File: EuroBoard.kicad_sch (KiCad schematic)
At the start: 35 parts, among them J1 GPIO, J10 PD1, J11 PD2, J12 PD3, J2 Conn_01x07_Male, J3 I2C, J4 Conn_01x05_Male, J5 RX, J6 TX, J7 GND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

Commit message: Rework
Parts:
- removed C1, C7: C, Capacitor_SMD:C_0805_2012Metric_Pad1.18x1.45mm_HandSolder, symbol Device:C
- removed C11: 10u, Capacitor_SMD:C_0805_2012Metric_Pad1.18x1.45mm_HandSolder, symbol Device:C
- removed C2, C8: 100n, Capacitor_SMD:C_0805_2012Metric_Pad1.18x1.45mm_HandSolder, symbol Device:C
- removed J1: GPIO, Connector_PinHeader_2.54mm:PinHeader_1x08_P2.54mm_Vertical, symbol Connector:Conn_01x08_Male
- removed J10: PD1, TestPoint:TestPoint_Pad_1.0x1.0mm, symbol Connector:Conn_01x01_Male
- removed J11: PD2, TestPoint:TestPoint_Pad_1.0x1.0mm, symbol Connector:Conn_01x01_Male
- removed J12: PD3, TestPoint:TestPoint_Pad_1.0x1.0mm, symbol Connector:Conn_01x01_Male
- removed J2: Conn_01x07_Male, Connector_PinHeader_2.54mm:PinHeader_1x07_P2.54mm_Vertical, symbol Connector:Conn_01x07_Male
- removed J3: I2C, Connector_PinHeader_2.54mm:PinHeader_1x03_P2.54mm_Vertical, symbol Connector:Conn_01x03_Male
- removed J4: Conn_01x05_Male, Connector_PinHeader_2.54mm:PinHeader_1x05_P2.54mm_Vertical, symbol Connector:Conn_01x05_Male
- removed J5: RX, TestPoint:TestPoint_Pad_1.0x1.0mm, symbol Connector:Conn_01x01_Male
- removed J6: TX, TestPoint:TestPoint_Pad_1.0x1.0mm, symbol Connector:Conn_01x01_Male
- removed J7: GND, TestPoint:TestPoint_Pad_1.0x1.0mm, symbol Connector:Conn_01x01_Male
- removed R1: R, Resistor_SMD:R_0805_2012Metric_Pad1.20x1.40mm_HandSolder, symbol Device:R
- removed R2: 1k, Resistor_SMD:R_0805_2012Metric_Pad1.20x1.40mm_HandSolder, symbol Device:R
- added C1, C5: 8p, Capacitor_SMD:C_0805_2012Metric_Pad1.18x1.45mm_HandSolder, symbol Device:C_Small
- added C2, C7: 100n, Capacitor_SMD:C_0805_2012Metric_Pad1.18x1.45mm_HandSolder, symbol Device:C_Small
- added C8: 10u, Capacitor_SMD:C_0805_2012Metric_Pad1.18x1.45mm_HandSolder, symbol Device:C_Small
- added R1, R2, R4: 0R, Capacitor_SMD:C_0805_2012Metric_Pad1.18x1.45mm_HandSolder, symbol Device:R_Small
- added R5: 1k, Resistor_SMD:R_0805_2012Metric_Pad1.20x1.40mm_HandSolder, symbol Device:R_Small
- added TP1: SPI1_SCK, MEMS_Custom:TestPoint_Pad_D1.0mm, symbol Connector:TestPoint
- added TP10: GP0, MEMS_Custom:TestPoint_Pad_D1.0mm, symbol Connector:TestPoint
- added TP11, TP12, TP13, TP14, TP15: GND, MEMS_Custom:TestPoint_Pad_D1.0mm, symbol Connector:TestPoint
- added TP16: 3V3, MEMS_Custom:TestPoint_Pad_D1.0mm, symbol Connector:TestPoint
- added TP2: SPI1_MISO, MEMS_Custom:TestPoint_Pad_D1.0mm, symbol Connector:TestPoint
- added TP3: SPI1_MOSI, MEMS_Custom:TestPoint_Pad_D1.0mm, symbol Connector:TestPoint
- added TP4: SCL_INT, MEMS_Custom:TestPoint_Pad_D1.0mm, symbol Connector:TestPoint
- added TP5: SDA_INT, MEMS_Custom:TestPoint_Pad_D1.0mm, symbol Connector:TestPoint
- added TP6: TRG, MEMS_Custom:TestPoint_Pad_D1.0mm, symbol Connector:TestPoint
- added TP7: RDY, MEMS_Custom:TestPoint_Pad_D1.0mm, symbol Connector:TestPoint
- added TP8: GP2, MEMS_Custom:TestPoint_Pad_D1.0mm, symbol Connector:TestPoint
- added TP9: GP1, MEMS_Custom:TestPoint_Pad_D1.0mm, symbol Connector:TestPoint
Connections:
- net SCL2 is gone; now on net GP2: U2.22 (PB10)
- net SDA2 is gone; now on net GP1: U2.23 (PB11)
- net +3.3V: now also C4.1, C6.1, L1.1, U1.2 (VO), TP16.1; no longer L1.2, U2.4 (VBAT), U2.6 (VDD/VDDA)
- net GND: now also C1.2, C2.2, C5.2, C7.2, C8.2, TP11.1, TP12.1, TP13.1, TP14.1, TP15.1
- net GP0: now also U2.24 (PB12), TP10.1; no longer U2.33 (PA11)
- net GP1: now also TP9.1; no longer U2.34 (PA12)
- net GP2: now also TP8.1; no longer U2.21 (PB2)
- net RDY: now also U2.48 (PB9), TP7.1; no longer U2.20 (PB1)
- net SPI1_MISO: now also TP2.1
- net SPI1_MOSI: now also TP3.1
- net SPI1_SCK: now also U2.16 (PA5), TP1.1; no longer U2.12 (PA1)
- net TRG: now also U2.47 (PB8), TP6.1; no longer U2.19 (PB0)
- net at D2.2 (A), SW1.2 (B), U2.10 (NRST): now also C2.1
- net PA0: now reaches U2.11 (PA0)
- net PA4: now reaches U2.15 (PA4)
- net at D1.2 (A): now also R5.1
- net at U2.2 (OSC32_IN/PC14): now also Y1.3, C1.1
- net at SW2.4: now also U2.38 (PD0); no longer U2.24 (PB12)
- net at SW2.3: now also U2.39 (PD1); no longer U2.25 (PB13)
- net at SW2.2: now also U2.40 (PD2); no longer U2.26 (PB14)
- net at SW2.1: now also U2.41 (PD3); no longer U2.27 (PB15)
- net PA8: now reaches U2.28 (PA8)
- net at U2.3 (OSC32_OUT/PC15): now also R4.2
- net PB6: now reaches U2.30 (PC6)
- net at U2.31 (PC7): now also R5.2
- net PA15: now reaches U2.37 (PA15)
- net PB3: now reaches U2.42 (PB3)
- net PB4: now reaches U2.43 (PB4)
- net PB5: now reaches U2.44 (PB5)
- net at Y1.1: now also C5.1, R4.1
- net LED renamed PC13
- net OSC_IN renamed PF0
- net PF0: no longer Y1.3
- net OSC_OUT renamed PF1
- net RX_AUX renamed PA10
- net SCL renamed SCL_EXT
- net SCL_EXT: now also R1.1
- net SDA renamed SDA_EXT
- net SDA_EXT: now also R2.2
- net TX_AUX renamed PA9
- net VREF: no longer names the net of U2.5 (VREF+)
- net VREF: now also C7.1
- new net: C8.1, L1.2, U2.4 (VBAT), U2.6 (VDD/VDDA)
- new net PA1: U2.12 (PA1)
- new net PB0: U2.19 (PB0)
- new net PB1: U2.20 (PB1)
- new net PB2: U2.21 (PB2)
- new net SCL_INT: R1.2, TP4.1, U2.33 (PA11)
- new net SDA_INT: R2.1, TP5.1, U2.34 (PA12)
- new net SPI2_MISO: U2.26 (PB14)
- new net SPI2_MOSI: U2.27 (PB15)
- new net SPI2_SCK: U2.25 (PB13)
- no-connect marks 0 -> 2
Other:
- note added: "Connector"
- note added: "MISC"
- note added: "Power Supply"
- title: (none) -> EuroMeasure-Module
- moved on the sheet: C12, C13, C14, C15, C3, C4, C6, C9, D1, D2, F1, L1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

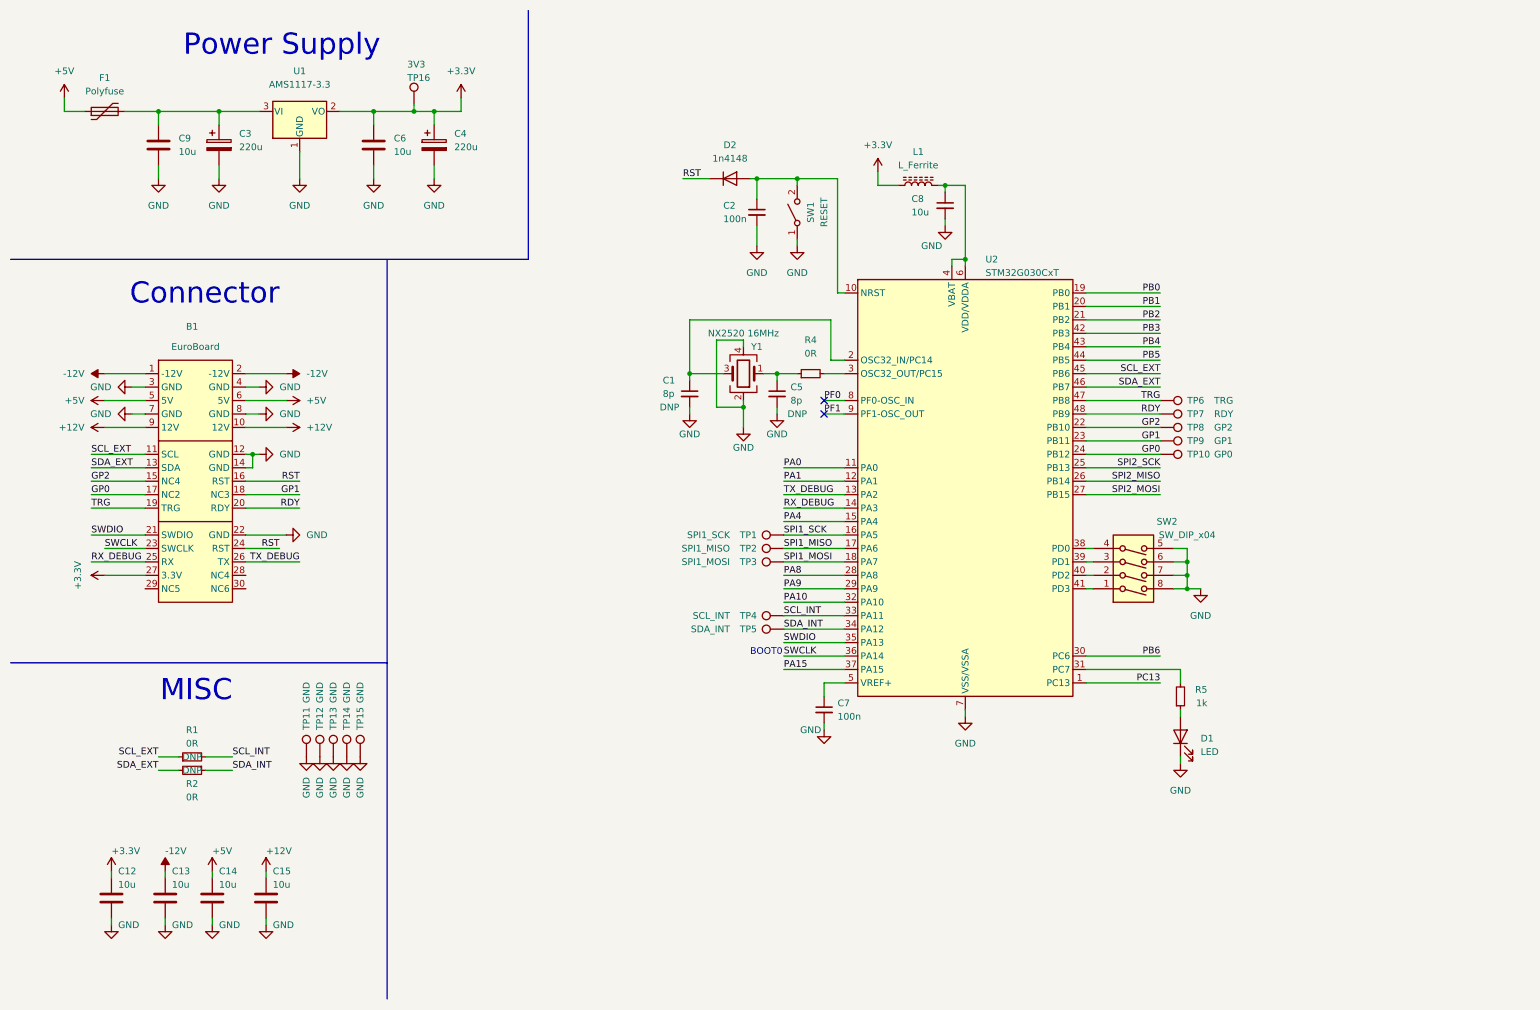
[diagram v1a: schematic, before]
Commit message: Added jumpers for address selection
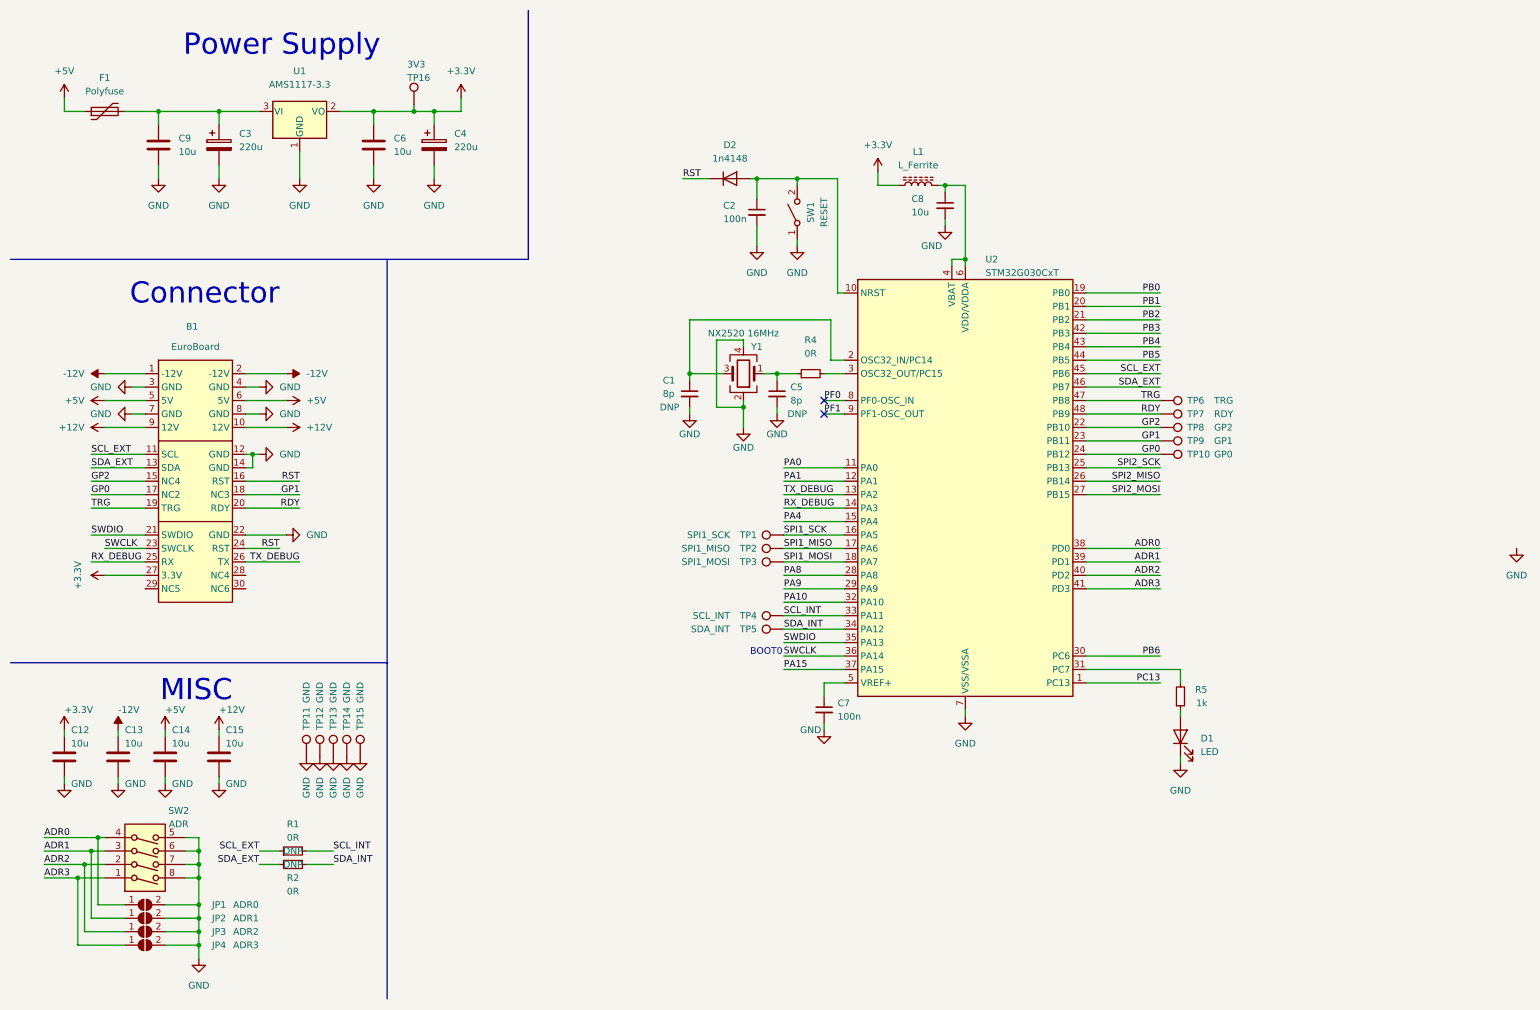
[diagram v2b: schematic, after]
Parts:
- added JP1: ADR0, MEMS_Passive:R_0805_2012Metric_Jumper, symbol Jumper:SolderJumper_2_Open
- added JP2: ADR1, MEMS_Passive:R_0805_2012Metric_Jumper, symbol Jumper:SolderJumper_2_Open
- added JP3: ADR2, MEMS_Passive:R_0805_2012Metric_Jumper, symbol Jumper:SolderJumper_2_Open
- added JP4: ADR3, MEMS_Passive:R_0805_2012Metric_Jumper, symbol Jumper:SolderJumper_2_Open
- SW2: value SW_DIP_x04 -> ADR
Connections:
- net GND: now also JP1.2 (B), JP2.2 (B), JP3.2 (B), JP4.2 (B)
- net ADR0: now reaches SW2.4, U2.38 (PD0)
- net ADR0: now also JP1.1 (A)
- net ADR1: now reaches SW2.3, U2.39 (PD1)
- net ADR1: now also JP2.1 (A)
- net ADR2: now reaches SW2.2, U2.40 (PD2)
- net ADR2: now also JP3.1 (A)
- net ADR3: now reaches SW2.1, U2.41 (PD3)
- net ADR3: now also JP4.1 (A)
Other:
- moved on the sheet: C12, C13, C14, C15, R1, R2, SW2

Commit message: Fixed pin numbering error
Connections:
- net PB6 renamed PC6
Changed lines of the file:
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@@
     (effects (font (size 1.27 1.27)) (justify left bottom))
   )
-  (label "PB6" (at 228.6 133.35 180)
+  (label "PC6" (at 228.6 133.35 180)
     (effects (font (size 1.27 1.27)) (justify right bottom))
   )

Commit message: Changed bus voltage from 12V to 15V
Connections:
- net +12V renamed +15V
- net -12V renamed -15V
- no-connect marks 2 -> 5
